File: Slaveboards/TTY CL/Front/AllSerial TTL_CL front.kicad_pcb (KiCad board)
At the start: 2 copper layers, 71.5 x 24 mm, 5 parts

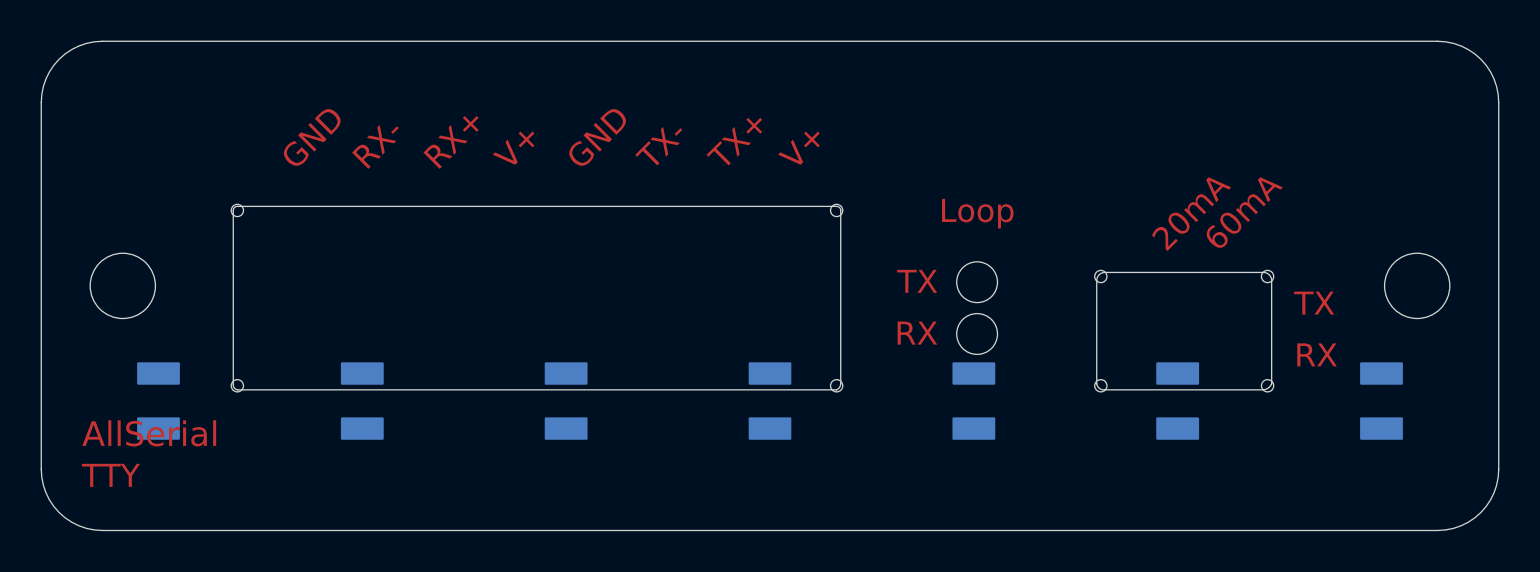
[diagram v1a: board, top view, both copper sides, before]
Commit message: Update TTY CL slave board
Add ESP32 S3 WiFi MasterBoard
Update libs
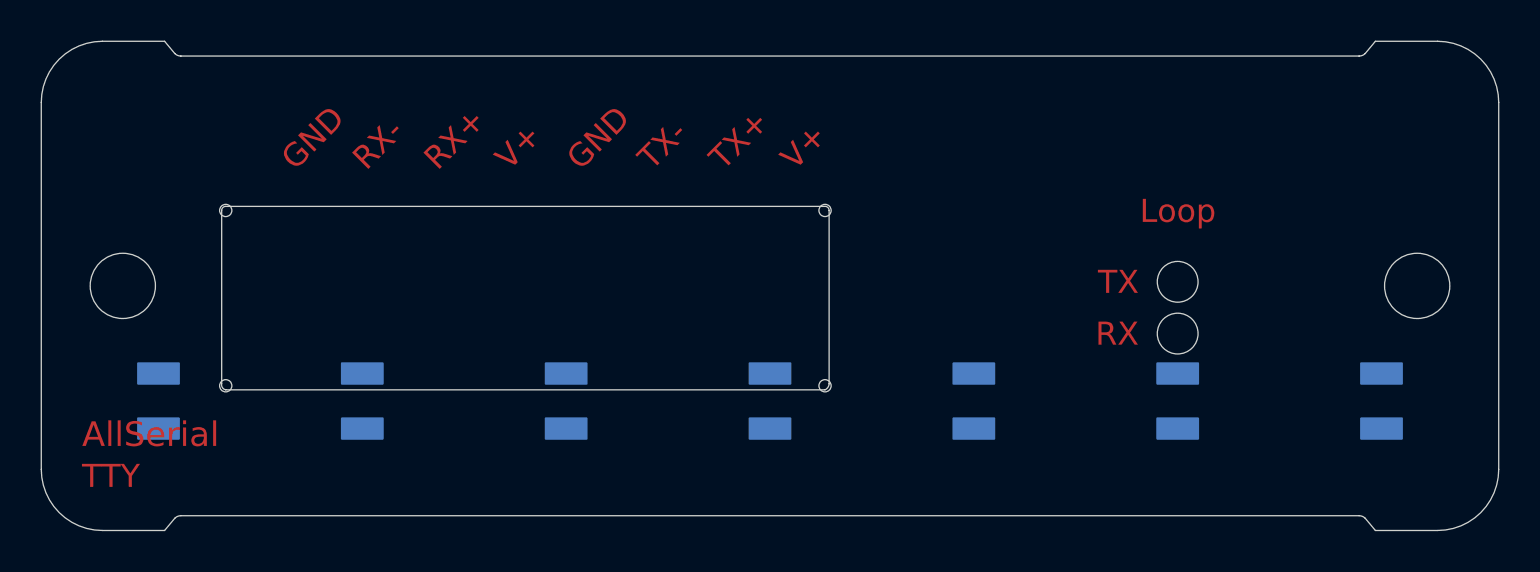
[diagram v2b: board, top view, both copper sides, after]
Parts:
- removed E$3: , 5_TTY_Front:LSTB-03-2
- moved @HOLE0 9.84 mm to (168.5, 107.3)
- moved @HOLE1 9.84 mm to (168.5, 104.8)
- moved E$2 0.57 mm to (136.5, 117.0)
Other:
- outline, holes or cut-outs redrawn
- board text added: "AllSerial TTY current loop - v2.0 46/18"
- board text added: "JLCJLCJLCJLC"
- board text removed: "20mA"
- board text removed: "60mA"
- board text removed: "AllSerial current loop - v1.2 46/18"

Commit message: Improve libraries
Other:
- outline, holes or cut-outs redrawn
- board text added: "CC1"
- board text added: "CC2"
- board text removed: "V+"

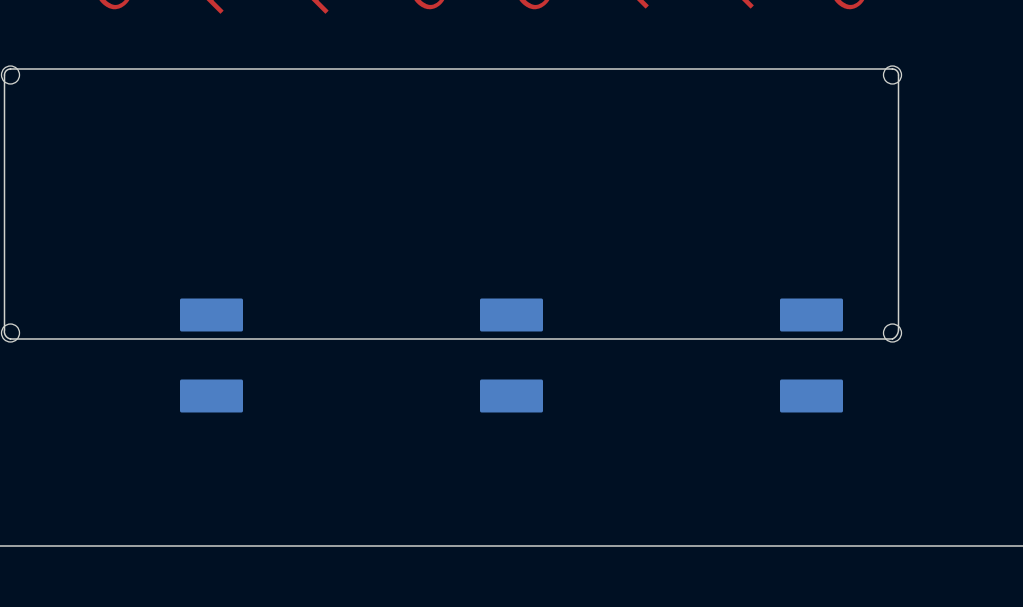
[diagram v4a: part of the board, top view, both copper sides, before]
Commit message: Remove pads from cutouts
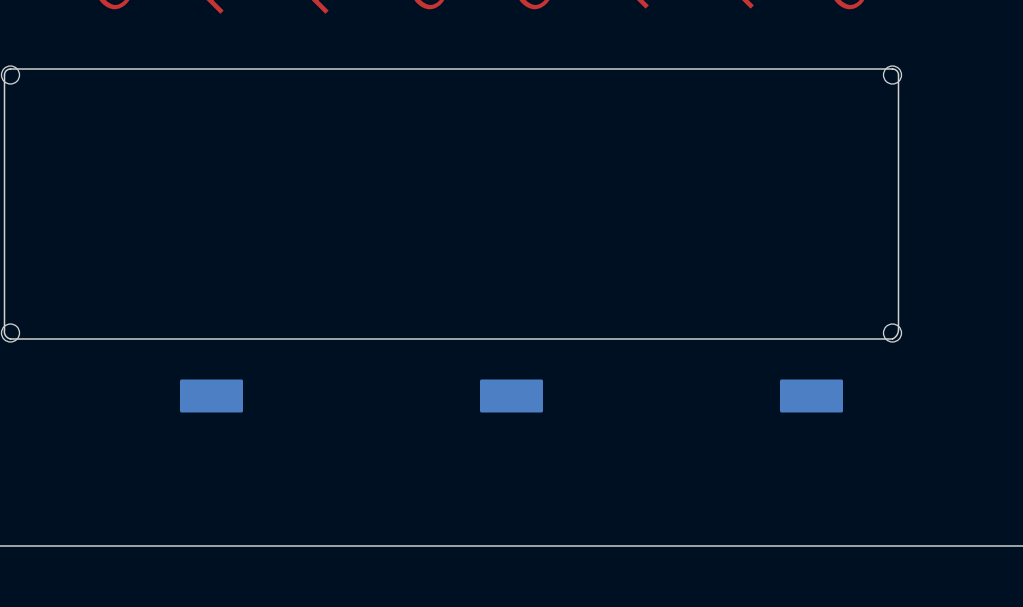
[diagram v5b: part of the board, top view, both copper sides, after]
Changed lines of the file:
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@@
-		)
-		(fp_rect
-			(start -21 -8.2)
-			(end -19 -7.2)
-			(stroke
-				(width 0.1)
-				(type solid)
-			)
-			(fill yes)
-			(layer "B.Cu")
 		)
 		(fp_rect
@@
 		)
 		(fp_rect
-			(start -11 -8.2)
-			(end -9 -7.2)
-			(stroke
-				(width 0.1)
-				(type solid)
-			)
-			(fill yes)
-			(layer "B.Cu")
-		)
-		(fp_rect
 			(start -11 -5.5)
 			(end -9 -4.5)
-			(stroke
-				(width 0.1)
-				(type solid)
-			)
-			(fill yes)
-			(layer "B.Cu")
-		)
-		(fp_rect
-			(start -1 -8.2)
-			(end 1 -7.2)
 			(stroke
 				(width 0.1)
@@
 		)
 		(fp_rect
-			(start -21 -8.2)
+			(start -21 -5.6)
 			(end -19 -4.5)
 			(stroke
@@
 		)
 		(fp_rect
-			(start -11 -8.2)
+			(start -11 -5.6)
 			(end -9 -4.5)
 			(stroke
@@
 		)
 		(fp_rect
-			(start -1 -8.2)
+			(start -1 -5.55)
 			(end 1 -4.5)
 			(stroke

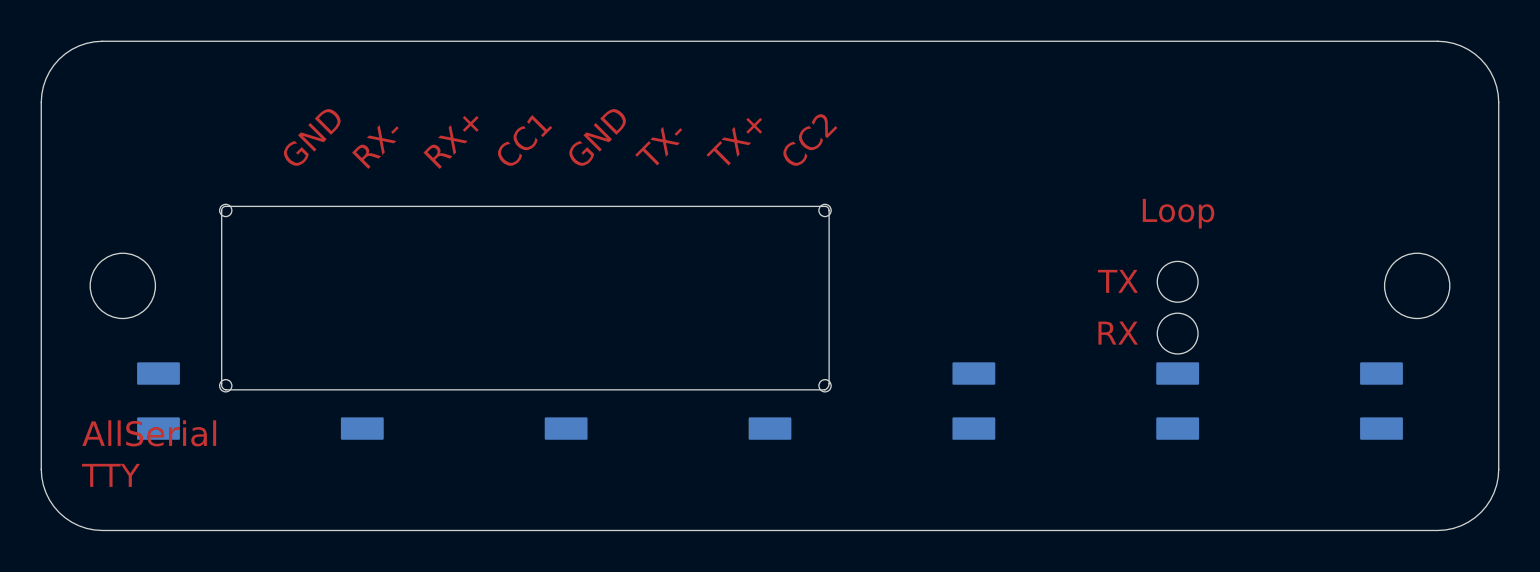
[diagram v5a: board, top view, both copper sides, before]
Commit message: Add python testskript
Add mainboard tester
Add libraries
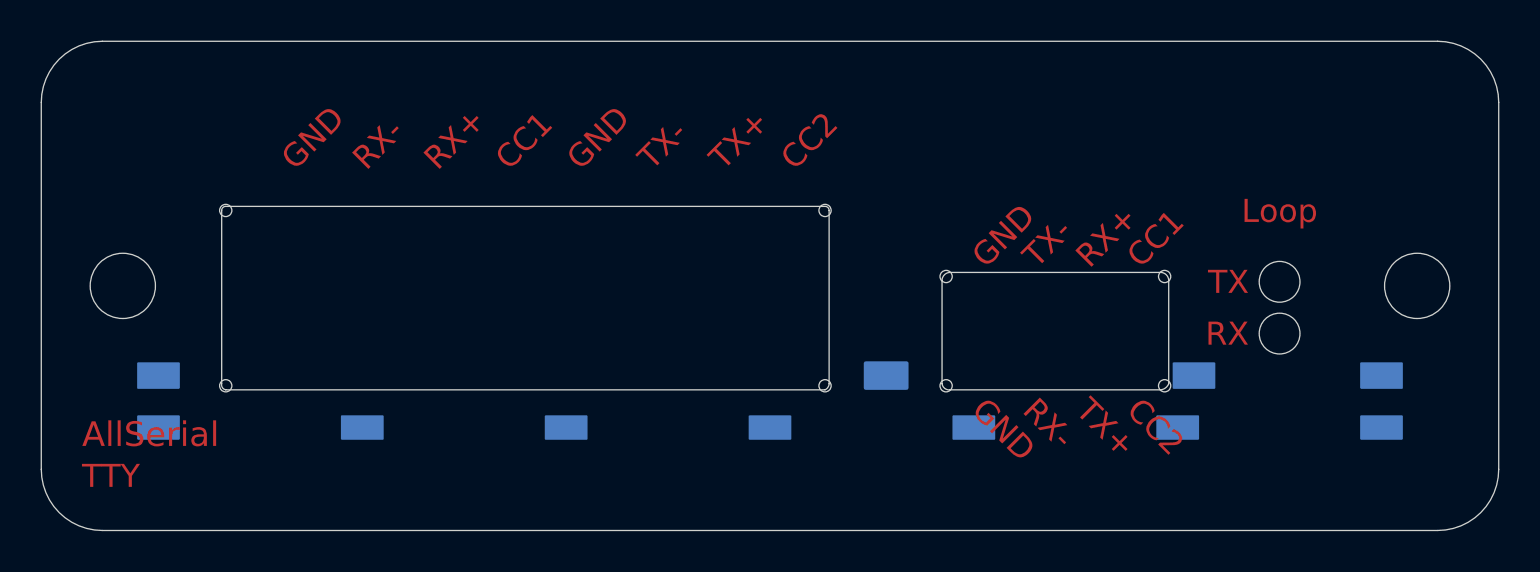
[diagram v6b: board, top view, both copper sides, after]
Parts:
- added REF**: Val**, AllSerial:Jumper_254_2x04, F.Cu at (162.5, 117.0)
- moved @HOLE0 5.00 mm to (173.5, 107.3)
- moved @HOLE1 5.00 mm to (173.5, 104.8)
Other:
- board text added: "AllSerial TTY current loop - v2.0 36/25"
- board text removed: "AllSerial TTY current loop - v2.0 46/18"
- board text removed: "JLCJLCJLCJLC"
